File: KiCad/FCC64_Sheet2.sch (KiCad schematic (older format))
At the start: 23 parts, among them SW1 Reset, U2 ATF1504AS, U3 W65C02S_TQFP, U4 ICS525-01, U5 27C256, U6 62256, U7 TPS3619-50, X1 12MHz

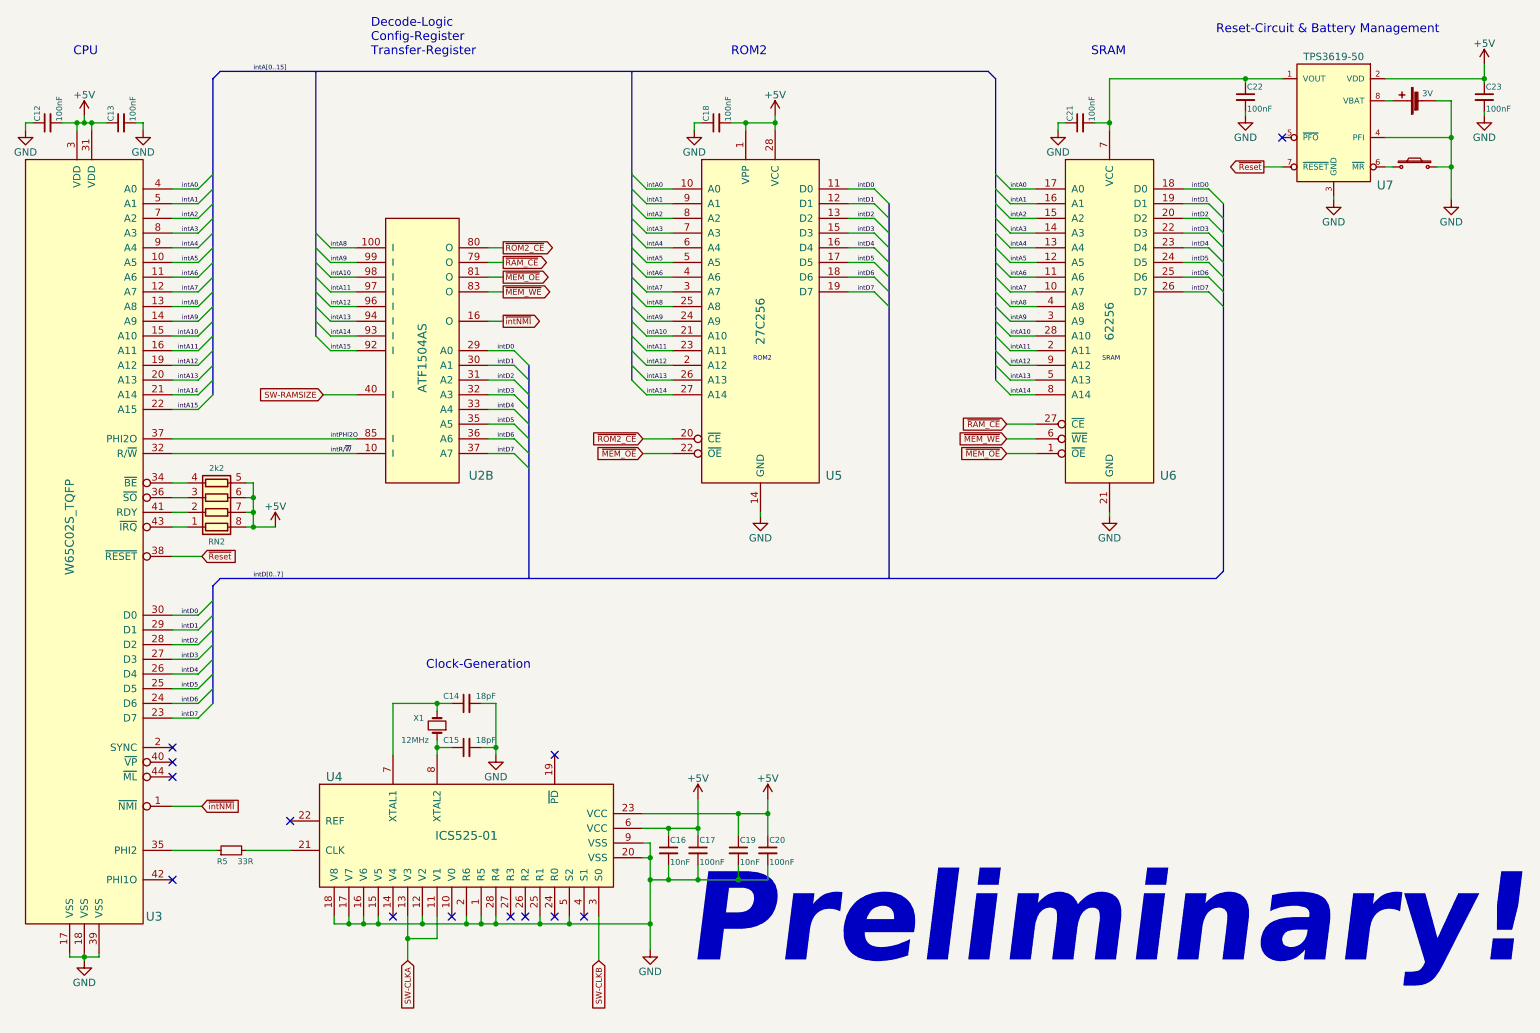
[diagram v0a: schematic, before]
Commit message: Various issues solved:
* QFP44-Footprint for W65C02 corrected
* FCC-On/Off deleted
* new battery supervisor ic TPS6513-01
* Battery Holder corrected
* Signals D5 and D7 to CPLD swapped
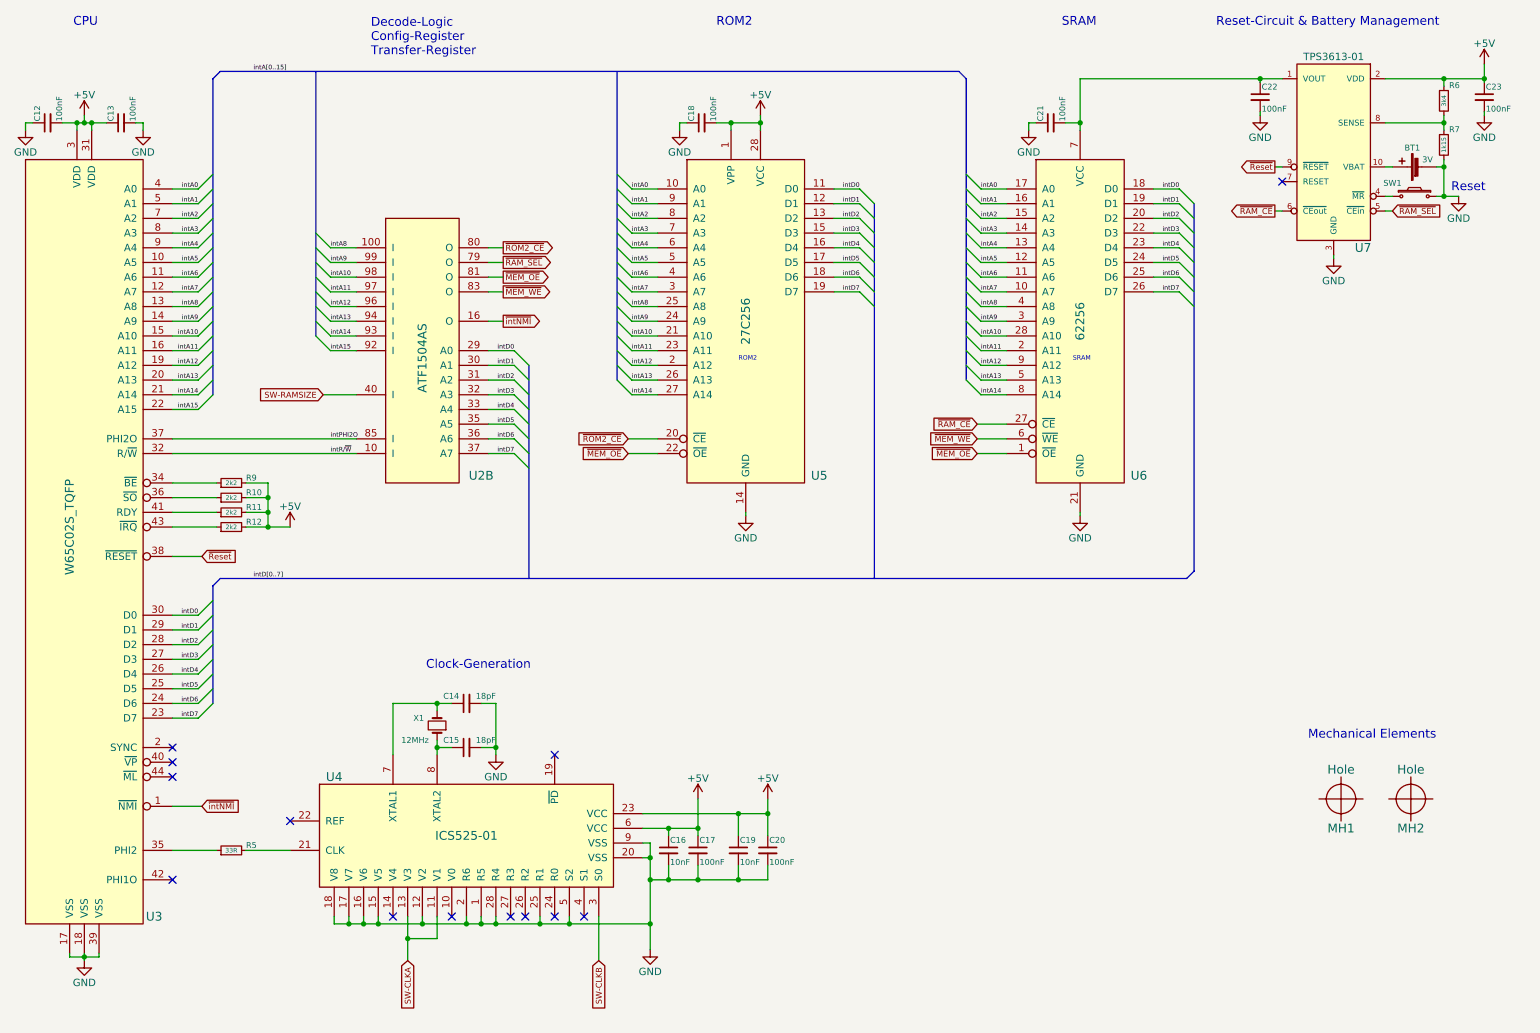
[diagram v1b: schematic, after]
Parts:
- removed RN2: 2k2, TTB_MyLib:TTB_RNet1206_4R, symbol R_Pack04
- removed U2: ATF1504AS, symbol ATF1504
- removed U7: TPS3619-50, Housings_DFN_QFN:DFN-8_2x2mm_Pitch0.5mm, symbol TPS3619-50
- added MH1: Hole, TTB_MyLib:TTB_Hole4,8mm, symbol Hole
- added MH2: Hole, TTB_MyLib:TTB_Hole3,1mm, symbol Hole
- added R10, R11, R12, R9: 2k2, TTB_MyLib:TTB_R0603, symbol R_Small
- added R6: 3k4, TTB_MyLib:TTB_R0603, symbol R_Small
- added R7: 1k15, TTB_MyLib:TTB_R0603, symbol R_Small
- added U2: ATF1504AS, TTB_MyLib:TTB_TQFP100, symbol ATF1504-RESCUE-FCC64
- added U7: TPS3613-01, TTB_MyLib:TTB_MSOP10, symbol TPS3613-01
- U3: footprint Housings_QFP:TQFP-44_10x10mm_Pitch0.8mm -> TTB_MyLib:TTB_W65C02
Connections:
- net +5V: now also R10.2, R11.2, R12.2, R6.1, R9.2, U7.2 (VDD)
- net GND: now also R7.2, U7.3 (GND)
- net SW-RAMSIZE: now also U2.40 (I)
- net intA10: now also U2.98 (I)
- net intA11: now also U2.97 (I)
- net intA12: now also U2.96 (I)
- net intA13: now also U2.94 (I)
- net intA14: now also U2.93 (I)
- net intA15: now also U2.92 (I)
- net intA8: now also U2.100 (I)
- net intA9: now also U2.99 (I)
- net intD0: now also U2.29 (A0)
- net intD1: now also U2.30 (A1)
- net intD2: now also U2.31 (A2)
- net intD3: now also U2.32 (A3)
- net intD4: now also U2.33 (A4)
- net intD5: now also U2.35 (A5)
- net intD6: now also U2.36 (A6)
- net intD7: now also U2.37 (A7)
- net intPHI2O: now also U2.85 (I)
- net intR/~W: now also U2.10 (I)
- net ~MEM_OE: now also U2.81 (O)
- net ~MEM_WE: now also U2.83 (O)
- net ~RAM_CE: now also U7.6 (~CEout)
- net ~ROM2_CE: now also U2.80 (O)
- net ~Reset: now also U7.9 (~RESET)
- net ~intNMI: now also U2.16 (O)
- net at BT1.1 (+): now also U7.10 (VBAT)
- net at SW1.2: now also U7.4 (~MR)
- net at C21.2, C22.1, U6.7 (VCC): now also U7.1 (VOUT)
- net at U3.34 (~BE): now also R9.1
- net at U3.36 (~SO): now also R10.1
- net at U3.41 (RDY): now also R11.1
- net at U3.43 (~IRQ): now also R12.1
- new net: R6.2, R7.1, U7.8 (SENSE)
- new net ~RAM_SEL: U2.79 (O), U7.5 (~CEin)
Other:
- note added: "Mechanical Elements"
- note added: "Reset"
- note removed: "Preliminary!"
- moved on the sheet: C18, C21, C22, U5, U6
